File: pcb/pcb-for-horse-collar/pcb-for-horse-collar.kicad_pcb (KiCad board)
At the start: 2 copper layers, 29 parts, among them J1 Conn_01x02_Socket, P1 USB_C_Receptacle_USB2.0_16P, Q1 S8050, Q2 S8050, SW2 OS102011MS2Q, U1 ESP32-WROOM-32E, U2 BNO085, U3 CP2102N-Axx-xQFN28, U4 MCP73831-2-OT, U5 AP2112K-3.3

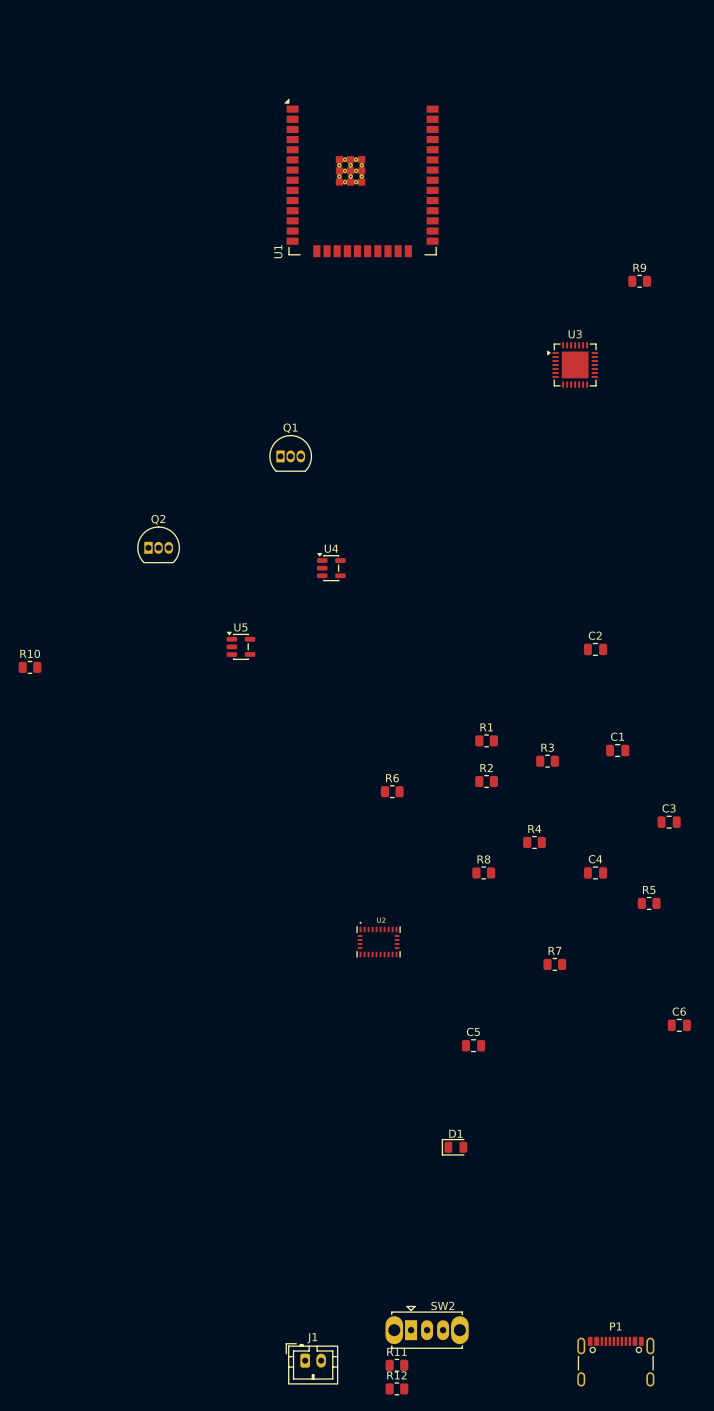
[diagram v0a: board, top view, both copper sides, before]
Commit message: New size for edges
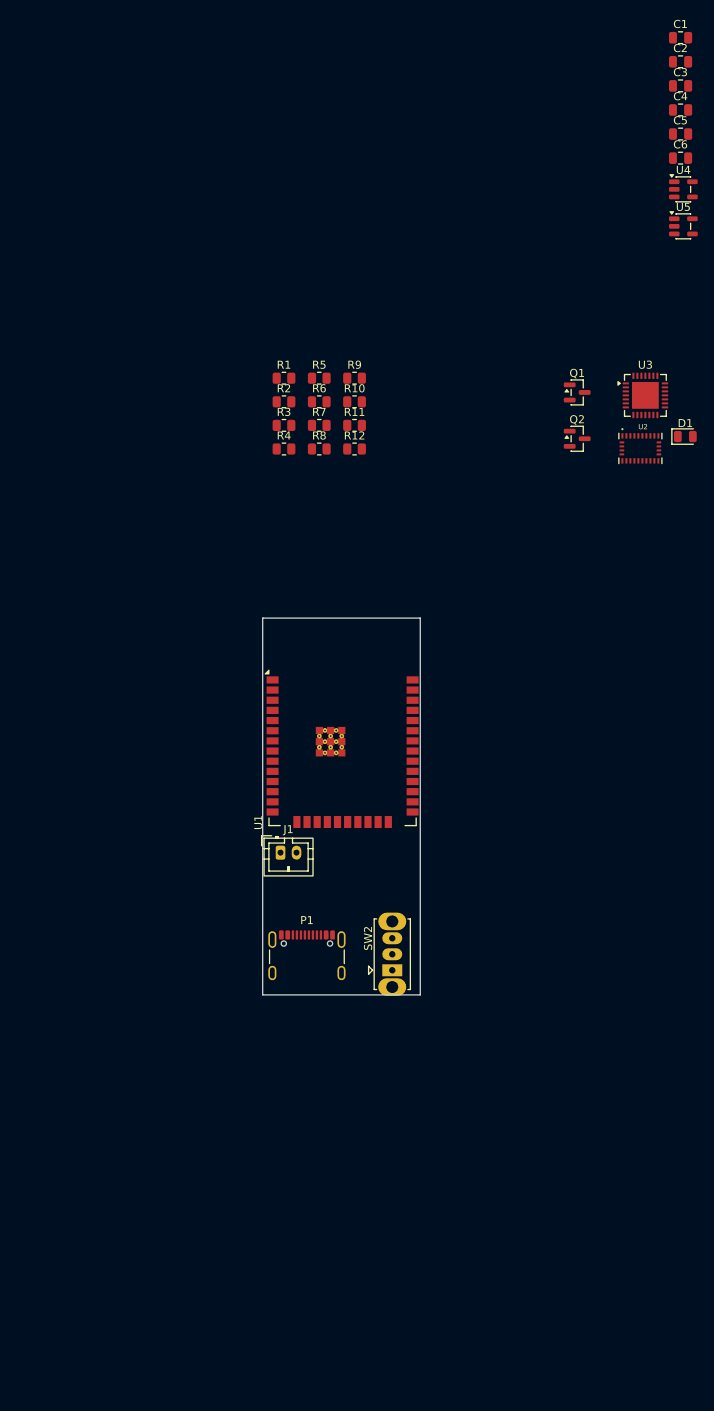
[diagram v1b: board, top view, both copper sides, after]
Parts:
- Q1, Q2: footprint Package_TO_SOT_THT:TO-92_Inline -> Package_TO_SOT_SMD:SOT-23
- moved R12 117.6 mm to (119.7, 77.8)
- moved R11 117.6 mm to (119.7, 74.9)
- moved C5 116.9 mm to (160.5, 38.4)
- moved C6 108.4 mm to (160.5, 41.5)
- moved C4 96.0 mm to (160.5, 35.4)
- moved D1 93.4 mm to (161.1, 76.3)
- moved C3 92.0 mm to (160.5, 32.4)
- moved C1 89.4 mm to (160.5, 26.4)
- moved R5 77.5 mm to (115.3, 69.0)
- moved U5 76.3 mm to (160.8, 50.0)
- moved C2 74.2 mm to (160.5, 29.4)
- moved R7 73.5 mm to (115.3, 74.9)
- moved U1 71.4 mm to (118.2, 111.9)
- moved U2 69.8 mm to (155.5, 77.7)
- moved U4 64.6 mm to (160.8, 45.4)
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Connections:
- P1 pad SH: unconnected-(P1-SHIELD-PadSH)_1 -> /unconnected-(P1-SHIELD-PadSH)_1_1
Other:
- board outline added: 19.7 x 47.1 mm
